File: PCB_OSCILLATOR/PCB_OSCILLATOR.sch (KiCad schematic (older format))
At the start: 12 parts

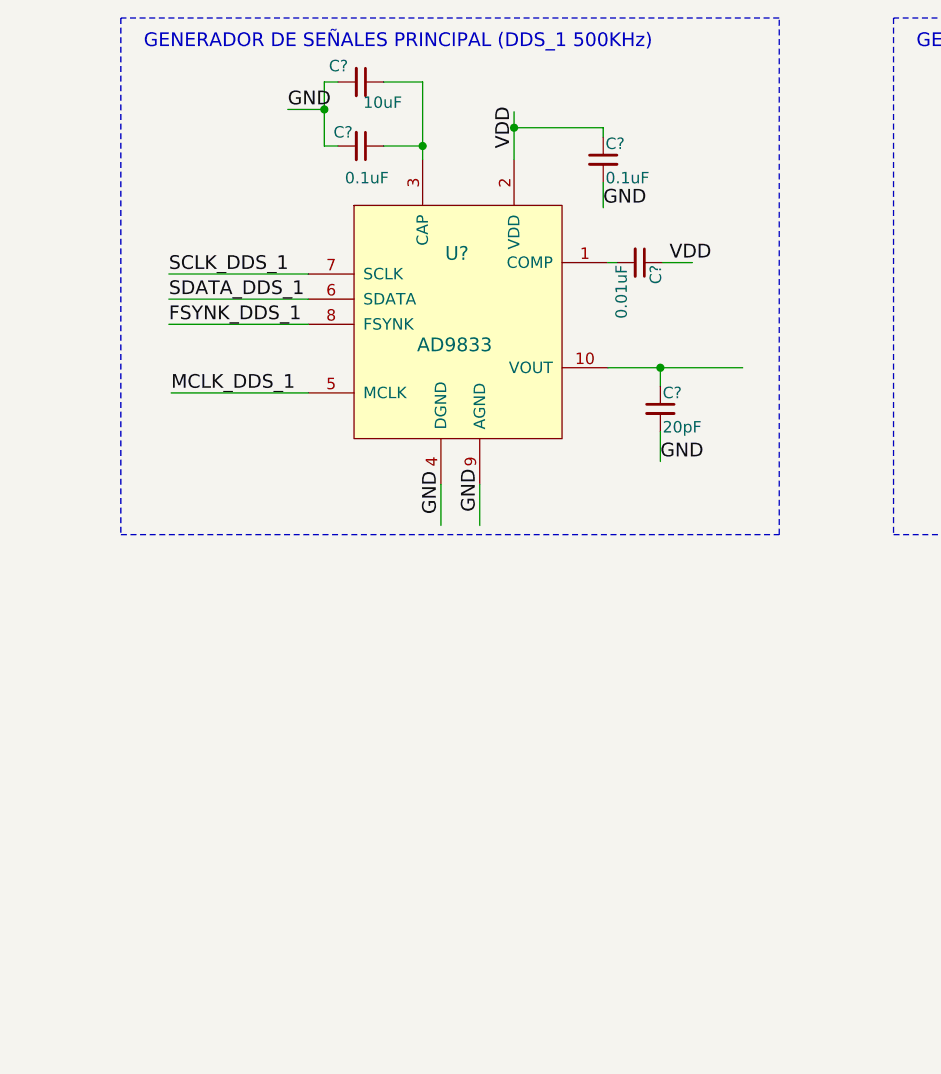
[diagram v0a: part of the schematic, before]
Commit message: MCLK+
Se agregan los osciladores para los MCLK de los DDS
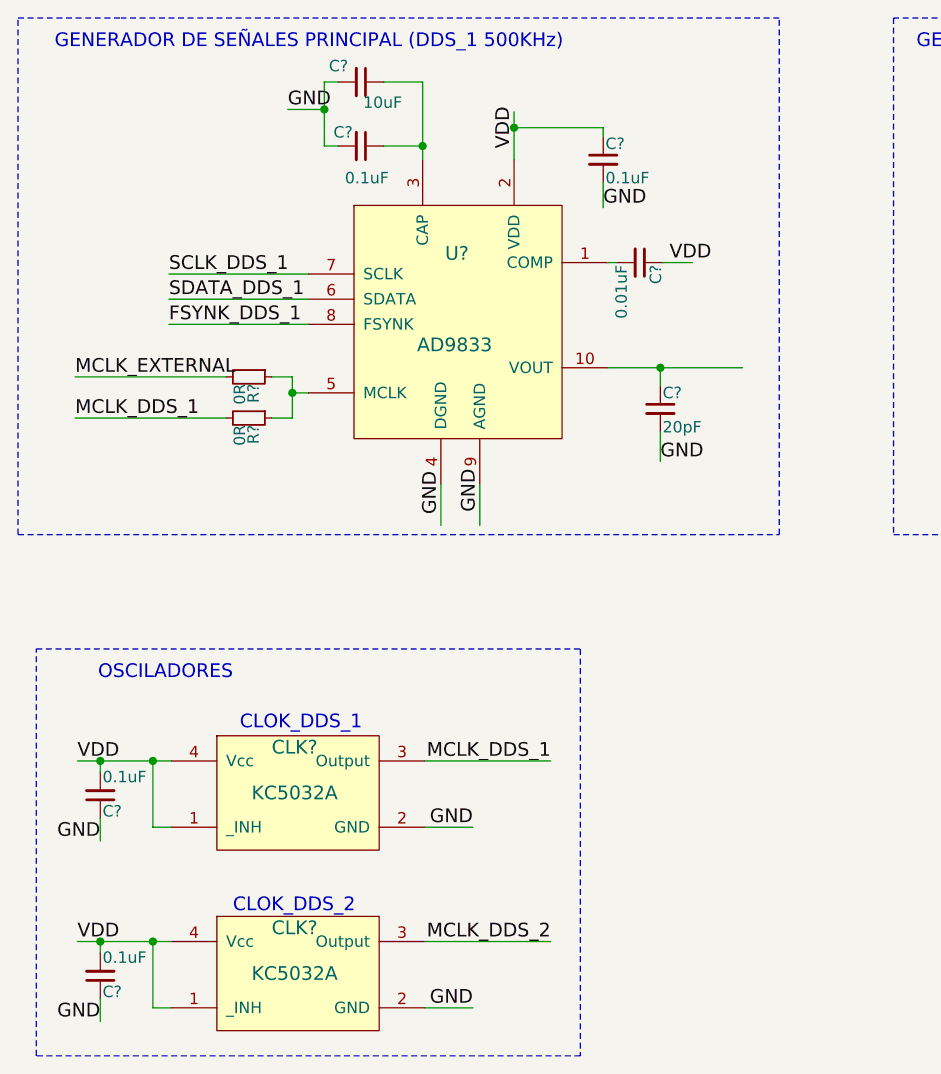
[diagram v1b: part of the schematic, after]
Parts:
- added C? (x2): 0.1uF, symbol C_Small
- added CLK? (x2): KC5032A, symbol KC5032A
- added R? (x2): 0R, symbol R_Small
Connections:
- net labels added: MCLK_EXTERNAL
- wire segments 44 -> 63
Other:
- note added: "CLOK_DDS_1"
- note added: "CLOK_DDS_2"
- note added: "OSCILADORES"
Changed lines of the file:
@@
 	1    0    0    -1
 $EndComp
-Wire Wire Line
-	1510 2200 2120 2200
-Wire Wire Line
-	1510 2310 2120 2310
-Wire Wire Line
-	1510 2420 2120 2420
-Wire Wire Line
-	1520 2720 2120 2720
-Wire Wire Line
-	2870 3120 2870 3300
-Wire Wire Line
-	2700 3120 2700 3300
 Text Label 2700 3250 1    60   ~ 0
 GND
@@
 	0    1    1    0
 $EndComp
-Wire Wire Line
-	3470 2150 3430 2150
-Wire Wire Line
-	3670 2150 3800 2150
 Text Label 3700 2150 0    60   ~ 0
 VDD
-Wire Wire Line
-	3020 1700 3020 1490
 Text Label 3020 1650 1    60   ~ 0
 VDD
@@
 	1    0    0    -1
 $EndComp
-Wire Wire Line
-	3410 1560 3410 1600
-Wire Wire Line
-	3410 1560 3020 1560
-Connection ~ 3020 1560
-Wire Wire Line
-	3410 1800 3410 1910
 Text Label 3410 1910 0    60   ~ 0
 GND
@@
 	0    1    1    0
 $EndComp
-Wire Wire Line
-	2450 1360 2620 1360
-Wire Wire Line
-	2620 1360 2620 1700
-Wire Wire Line
-	2450 1640 2620 1640
-Connection ~ 2620 1640
-Wire Wire Line
-	2250 1640 2190 1640
-Wire Wire Line
-	2190 1640 2190 1360
-Wire Wire Line
-	2190 1360 2250 1360
-Wire Wire Line
-	2190 1480 2030 1480
-Connection ~ 2190 1480
 Text Label 2030 1480 0    60   ~ 0
 GND
-Text Label 1520 2720 0    60   ~ 0
-MCLK_DDS_1
 Text Label 1510 2200 0    60   ~ 0
 SCLK_DDS_1
@@
 Text Label 1510 2420 0    60   ~ 0
 FSYNK_DDS_1
-Wire Wire Line
-	3430 2610 4020 2610
 $Comp
 L C_Small C?
@@
 	1    0    0    -1
 $EndComp
-Wire Wire Line
-	3660 2690 3660 2610
-Connection ~ 3660 2610
-Wire Wire Line
-	3660 2890 3660 3020
 Text Label 3660 3020 0    60   ~ 0
 GND
-Text Notes 1400 1220 0    60   ~ 0
+Text Notes 1010 1220 0    60   ~ 0
 GENERADOR DE SEÑALES PRINCIPAL (DDS_1 500KHz)\n
-Wire Notes Line
-	1300 1080 1300 3340
-Wire Notes Line
-	1300 3340 4180 3340
-Wire Notes Line
-	4180 3340 4180 1080
-Wire Notes Line
-	4180 1080 1300 1080
 $Comp
 L AD9833 U?
@@
 	1    0    0    -1
 $EndComp
-Wire Wire Line
-	4890 2200 5500 2200
-Wire Wire Line
-	4890 2310 5500 2310
-Wire Wire Line
-	4890 2420 5500 2420
-Wire Wire Line
-	4890 2720 5500 2720
-Wire Wire Line
-	6250 3120 6250 3300
-Wire Wire Line
-	6080 3120 6080 3300
 Text Label 6080 3250 1    60   ~ 0
 GND
@@
 	0    1    1    0
 $EndComp
-Wire Wire Line
-	6850 2150 6810 2150
-Wire Wire Line
-	7050 2150 7180 2150
 Text Label 7080 2150 0    60   ~ 0
 VDD
-Wire Wire Line
-	6400 1700 6400 1490
 Text Label 6400 1650 1    60   ~ 0
 VDD
@@
 	1    0    0    -1
 $EndComp
-Wire Wire Line
-	6790 1560 6790 1600
-Wire Wire Line
-	6790 1560 6400 1560
-Connection ~ 6400 1560
-Wire Wire Line
-	6790 1800 6790 1910
 Text Label 6790 1910 0    60   ~ 0
 GND
@@
 	0    1    1    0
 $EndComp
-Wire Wire Line
-	5830 1360 6000 1360
-Wire Wire Line
-	6000 1360 6000 1700
-Wire Wire Line
-	5830 1640 6000 1640
-Connection ~ 6000 1640
-Wire Wire Line
-	5630 1640 5570 1640
-Wire Wire Line
-	5570 1640 5570 1360
-Wire Wire Line
-	5570 1360 5630 1360
-Wire Wire Line
-	5570 1480 5410 1480
-Connection ~ 5570 1480
 Text Label 5410 1480 0    60   ~ 0
 GND
@@
 Text Label 4890 2420 0    60   ~ 0
 FSYNK_DDS_2
-Wire Wire Line
-	6810 2610 7400 2610
 $Comp
 L C_Small C?
@@
 	1    0    0    -1
 $EndComp
+Text Label 7040 3020 0    60   ~ 0
+GND
+Text Notes 4780 1220 0    60   ~ 0
+GENERADOR DE SEÑALES AUXILIAR (DDS_2 4KHz)\n
+$Comp
+L KC5032A CLK?
+U 1 1 590CEFAE
+P 2060 4470
+F 0 "CLK?" H 2060 4670 60  0000 C CNN
+F 1 "KC5032A" H 2060 4470 60  0000 C CNN
+F 2 "" H 2000 4480 60  0000 C CNN
+F 3 "" H 2000 4480 60  0000 C CNN
+	1    2060 4470
+	1    0    0    -1
+$EndComp
+Text Label 1110 4330 0    60   ~ 0
+VDD
+$Comp
+L C_Small C?
+U 1 1 590CFF1F
+P 1210 4480
+F 0 "C?" H 1220 4550 50  0000 L CNN
+F 1 "0.1uF" H 1220 4400 50  0000 L CNN
+F 2 "" H 1210 4480 50  0000 C CNN
+F 3 "" H 1210 4480 50  0000 C CNN
+	1    1210 4480
+	1    0    0    1
+$EndComp
+Wire Wire Line
+	1510 2200 2120 2200
+Wire Wire Line
+	1510 2310 2120 2310
+Wire Wire Line
+	1510 2420 2120 2420
+Wire Wire Line
+	2870 3120 2870 3300
+Wire Wire Line
+	2700 3120 2700 3300
+Wire Wire Line
+	3470 2150 3430 2150
+Wire Wire Line
+	3670 2150 3800 2150
+Wire Wire Line
+	3020 1700 3020 1490
+Wire Wire Line
+	3410 1560 3410 1600
+Wire Wire Line
+	3410 1560 3020 1560
+Connection ~ 3020 1560
+Wire Wire Line
+	3410 1800 3410 1910
+Wire Wire Line
+	2450 1360 2620 1360
+Wire Wire Line
+	2620 1360 2620 1700
+Wire Wire Line
+	2450 1640 2620 1640
+Connection ~ 2620 1640
+Wire Wire Line
+	2250 1640 2190 1640
+Wire Wire Line
+	2190 1640 2190 1360
+Wire Wire Line
+	2190 1360 2250 1360
+Wire Wire Line
+	2190 1480 2030 1480
+Connection ~ 2190 1480
+Wire Wire Line
+	3430 2610 4020 2610
+Wire Wire Line
+	3660 2690 3660 2610
+Connection ~ 3660 2610
+Wire Wire Line
+	3660 2890 3660 3020
+Wire Notes Line
+	850  3340 4180 3340
+Wire Notes Line
+	4180 3340 4180 1080
+Wire Notes Line
+	4180 1080 1300 1080
+Wire Wire Line
+	4890 2200 5500 2200
+Wire Wire Line
+	4890 2310 5500 2310
+Wire Wire Line
+	4890 2420 5500 2420
+Wire Wire Line
+	4890 2720 5500 2720
+Wire Wire Line
+	6250 3120 6250 3300
+Wire Wire Line
+	6080 3120 6080 3300
+Wire Wire Line
+	6850 2150 6810 2150
+Wire Wire Line
+	7050 2150 7180 2150
+Wire Wire Line
+	6400 1700 6400 1490
+Wire Wire Line
+	6790 1560 6790 1600
+Wire Wire Line
+	6790 1560 6400 1560
+Connection ~ 6400 1560
+Wire Wire Line
+	6790 1800 6790 1910
+Wire Wire Line
+	5830 1360 6000 1360
+Wire Wire Line
+	6000 1360 6000 1700
+Wire Wire Line
+	5830 1640 6000 1640
+Connection ~ 6000 1640
+Wire Wire Line
+	5630 1640 5570 1640
+Wire Wire Line
+	5570 1640 5570 1360
+Wire Wire Line
+	5570 1360 5630 1360
+Wire Wire Line
+	5570 1480 5410 1480
+Connection ~ 5570 1480
+Wire Wire Line
+	6810 2610 7400 2610
 Wire Wire Line
 	7040 2690 7040 2610
@@
 Wire Wire Line
 	7040 2890 7040 3020
-Text Label 7040 3020 0    60   ~ 0
-GND
-Text Notes 4780 1220 0    60   ~ 0
-GENERADOR DE SEÑALES AUXILIAR (DDS_2 4KHz)\n
 Wire Notes Line
 	4680 1080 4680 3340
@@
 Wire Notes Line
 	7560 1080 4680 1080
+Wire Wire Line
+	1110 4330 1520 4330
+Wire Wire Line
+	2630 4330 3180 4330
+Wire Wire Line
+	2630 4620 2840 4620
+Wire Wire Line
+	1440 4620 1520 4620
+Wire Wire Line
+	1440 4620 1440 4330
+Connection ~ 1440 4330
+Wire Wire Line
+	1210 4380 1210 4330
+Connection ~ 1210 4330
+Wire Wire Line
+	1210 4580 1210 4680
+Text Label 1210 4680 2    60   ~ 0
+GND
+Text Label 2840 4620 2    60   ~ 0
+GND
+Text Label 3180 4330 2    60   ~ 0
+MCLK_DDS_1
+$Comp
+L R_Small R?
+U 1 1 590D280D
+P 1860 2830
+F 0 "R?" H 1890 2850 50  0000 L CNN
+F 1 "0R" H 1890 2790 50  0000 L CNN
+F 2 "" H 1860 2830 50  0000 C CNN
+F 3 "" H 1860 2830 50  0000 C CNN
+	1    1860 2830
+	0    1    1    0
+$EndComp
+$Comp
+L R_Small R?
+U 1 1 590D28C6
+P 1860 2650
+F 0 "R?" H 1890 2670 50  0000 L CNN
+F 1 "0R" H 1890 2610 50  0000 L CNN
+F 2 "" H 1860 2650 50  0000 C CNN
+F 3 "" H 1860 2650 50  0000 C CNN
+	1    1860 2650
+	0    1    1    0
+$EndComp
+Wire Wire Line
+	2120 2720 2050 2720
+Wire Wire Line
+	1960 2650 2050 2650
+Wire Wire Line
+	2050 2650 2050 2830
+Wire Wire Line
+	2050 2830 1960 2830
+Connection ~ 2050 2720
+Wire Wire Line
+	1100 2650 1760 2650
+Wire Wire Line
+	1100 2830 1760 2830
+Text Label 1100 2830 0    60   ~ 0
+MCLK_DDS_1
+Text Label 1100 2650 0    60   ~ 0
+MCLK_EXTERNAL
+Wire Notes Line
+	850  3340 850  1080
+Wire Notes Line
+	850  1080 1310 1080
+$Comp
+L KC5032A CLK?
+U 1 1 590D5CFE
+P 2060 5260
+F 0 "CLK?" H 2060 5460 60  0000 C CNN
+F 1 "KC5032A" H 2060 5260 60  0000 C CNN
+F 2 "" H 2000 5270 60  0000 C CNN
+F 3 "" H 2000 5270 60  0000 C CNN
+	1    2060 5260
+	1    0    0    -1
+$EndComp
+Text Label 1110 5120 0    60   ~ 0
+VDD
+$Comp
+L C_Small C?
+U 1 1 590D5D05
+P 1210 5270
+F 0 "C?" H 1220 5340 50  0000 L CNN
+F 1 "0.1uF" H 1220 5190 50  0000 L CNN
+F 2 "" H 1210 5270 50  0000 C CNN
+F 3 "" H 1210 5270 50  0000 C CNN
+	1    1210 5270
+	1    0    0    1
+$EndComp
+Wire Wire Line
+	1110 5120 1520 5120
+Wire Wire Line
+	2630 5120 3180 5120
+Wire Wire Line
+	2630 5410 2840 5410
+Wire Wire Line
+	1440 5410 1520 5410
+Wire Wire Line
+	1440 5410 1440 5120
+Connection ~ 1440 5120
+Wire Wire Line
+	1210 5170 1210 5120
+Connection ~ 1210 5120
+Wire Wire Line
+	1210 5370 1210 5470
+Text Label 1210 5470 2    60   ~ 0
+GND
+Text Label 2840 5410 2    60   ~ 0
+GND
+Text Label 3180 5120 2    60   ~ 0
+MCLK_DDS_2
+Text Notes 1200 3980 0    60   ~ 0
+OSCILADORES
+Text Notes 1820 4200 0    60   ~ 0
+CLOK_DDS_1
+Text Notes 1790 5000 0    60   ~ 0
+CLOK_DDS_2
+Wire Notes Line
+	930  3840 3310 3840
+Wire Notes Line
+	3310 3840 3310 5620
+Wire Notes Line
+	3310 5620 930  5620
+Wire Notes Line
+	930  5620 930  3840
 $EndSCHEMATC

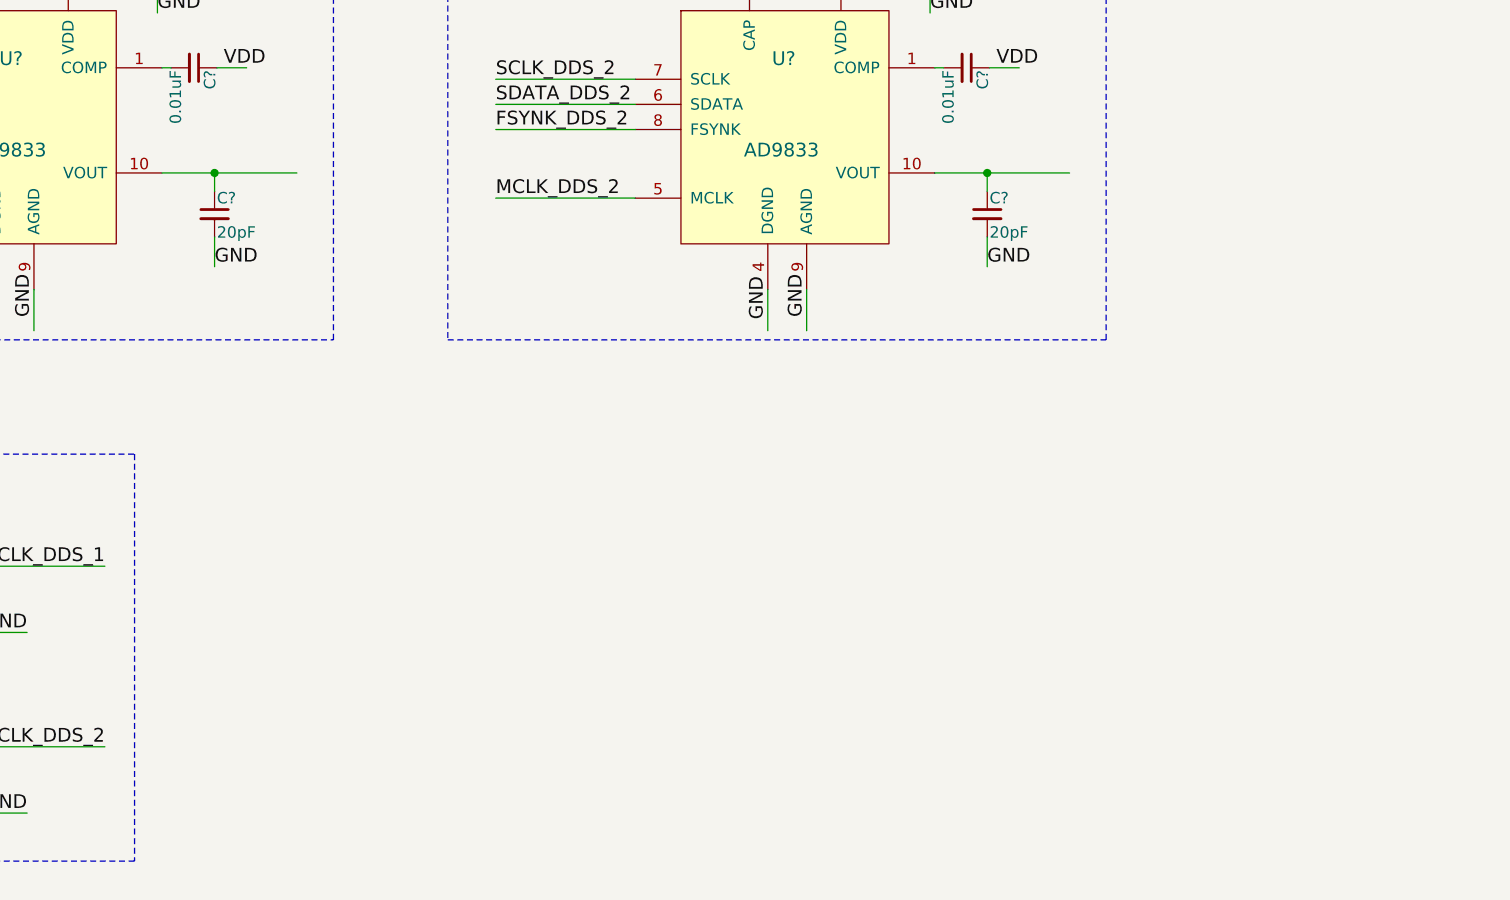
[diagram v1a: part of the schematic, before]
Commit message: AD8421_UPDATE
Se incluye la etapa de preamplificación y amplificación
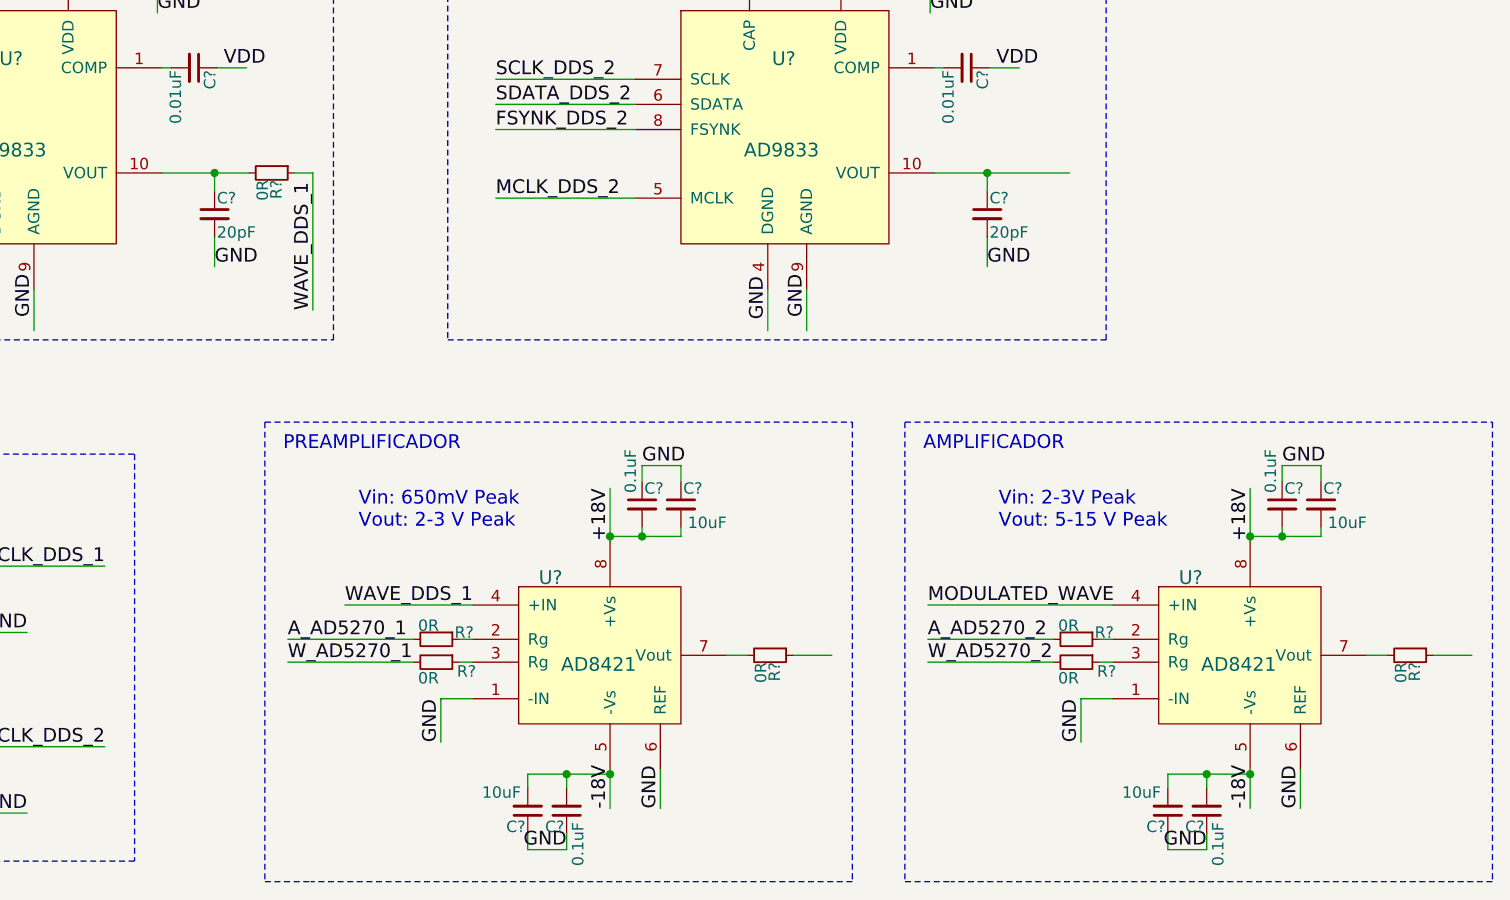
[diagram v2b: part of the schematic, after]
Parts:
- added C? (x4): 0.1uF, symbol C_Small
- added C? (x4): 10uF, symbol C_Small
- added R? (x7): 0R, symbol R_Small
- added U? (x2): AD8421, symbol AD8421
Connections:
- net labels added: +18V, -18V, A_AD5270_1, A_AD5270_2, MODULATED_WAVE, WAVE_DDS_1, W_AD5270_1, W_AD5270_2
- wire segments 63 -> 113
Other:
- note added: "AMPLIFICADOR"
- note added: "PREAMPLIFICADOR"
- note added: "Vin: 2-3V Peak\nVout: 5-15 V Peak"
- note added: "Vin: 650mV Peak\nVout: 2-3 V Peak"
